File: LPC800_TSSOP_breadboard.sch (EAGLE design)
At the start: 16 parts, among them Q1 12MHz

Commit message: * small fixes on TODO list
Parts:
- added C6: (no value), SquantorRCL:C-EUC0603K
- C2, C3: device bart_rcl:C-EUC0603 -> SquantorRCL:C-EUC0603K
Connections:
- net VDD: now also C6.1
- net VSS: now also C6.2
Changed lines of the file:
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@@
 <grid distance="0.1" unitdist="inch" unit="inch" style="lines" multiple="1" display="no" altdistance="0.01" altunitdist="inch" altunit="inch"/>
 <layers>
-<layer number="1" name="Top" color="4" fill="1" visible="yes" active="no"/>
-<layer number="16" name="Bottom" color="1" fill="1" visible="yes" active="no"/>
-<layer number="17" name="Pads" color="2" fill="1" visible="yes" active="no"/>
-<layer number="18" name="Vias" color="2" fill="1" visible="yes" active="no"/>
-<layer number="19" name="Unrouted" color="6" fill="1" visible="yes" active="no"/>
-<layer number="20" name="Dimension" color="15" fill="1" visible="yes" active="no"/>
-<layer number="21" name="tPlace" color="7" fill="1" visible="yes" active="no"/>
-<layer number="22" name="bPlace" color="7" fill="1" visible="yes" active="no"/>
-<layer number="23" name="tOrigins" color="15" fill="1" visible="yes" active="no"/>
-<layer number="24" name="bOrigins" color="15" fill="1" visible="yes" active="no"/>
-<layer number="25" name="tNames" color="7" fill="1" visible="yes" active="no"/>
-<layer number="26" name="bNames" color="7" fill="1" visible="yes" active="no"/>
-<layer number="27" name="tValues" color="7" fill="1" visible="yes" active="no"/>
-<layer number="28" name="bValues" color="7" fill="1" visible="yes" active="no"/>
+<layer number="1" name="Top" color="4" fill="1" visible="no" active="no"/>
+<layer number="16" name="Bottom" color="1" fill="1" visible="no" active="no"/>
+<layer number="17" name="Pads" color="2" fill="1" visible="no" active="no"/>
+<layer number="18" name="Vias" color="2" fill="1" visible="no" active="no"/>
+<layer number="19" name="Unrouted" color="6" fill="1" visible="no" active="no"/>
+<layer number="20" name="Dimension" color="15" fill="1" visible="no" active="no"/>
+<layer number="21" name="tPlace" color="7" fill="1" visible="no" active="no"/>
+<layer number="22" name="bPlace" color="7" fill="1" visible="no" active="no"/>
+<layer number="23" name="tOrigins" color="15" fill="1" visible="no" active="no"/>
+<layer number="24" name="bOrigins" color="15" fill="1" visible="no" active="no"/>
+<layer number="25" name="tNames" color="7" fill="1" visible="no" active="no"/>
+<layer number="26" name="bNames" color="7" fill="1" visible="no" active="no"/>
+<layer number="27" name="tValues" color="7" fill="1" visible="no" active="no"/>
+<layer number="28" name="bValues" color="7" fill="1" visible="no" active="no"/>
 <layer number="29" name="tStop" color="7" fill="3" visible="no" active="no"/>
 <layer number="30" name="bStop" color="7" fill="6" visible="no" active="no"/>
@@
 <layer number="35" name="tGlue" color="7" fill="4" visible="no" active="no"/>
 <layer number="36" name="bGlue" color="7" fill="5" visible="no" active="no"/>
-<layer number="37" name="tTest" color="7" fill="1" visible="yes" active="no"/>
-<layer number="38" name="bTest" color="7" fill="1" visible="yes" active="no"/>
+<layer number="37" name="tTest" color="7" fill="1" visible="no" active="no"/>
+<layer number="38" name="bTest" color="7" fill="1" visible="no" active="no"/>
 <layer number="39" name="tKeepout" color="4" fill="11" visible="no" active="no"/>
 <layer number="40" name="bKeepout" color="1" fill="11" visible="no" active="no"/>
@@
 <layer number="44" name="Drills" color="7" fill="1" visible="no" active="no"/>
 <layer number="45" name="Holes" color="7" fill="1" visible="no" active="no"/>
-<layer number="46" name="Milling" color="3" fill="1" visible="yes" active="no"/>
-<layer number="47" name="Measures" color="7" fill="1" visible="yes" active="no"/>
-<layer number="48" name="Document" color="7" fill="1" visible="yes" active="no"/>
-<layer number="49" name="Reference" color="7" fill="1" visible="yes" active="no"/>
-<layer number="50" name="dxf" color="7" fill="1" visible="yes" active="no"/>
-<layer number="51" name="tDocu" color="7" fill="1" visible="yes" active="no"/>
-<layer number="52" name="bDocu" color="7" fill="1" visible="yes" active="no"/>
-<layer number="53" name="tGND_GNDA" color="7" fill="9" visible="yes" active="no"/>
-<layer number="54" name="bGND_GNDA" color="1" fill="9" visible="yes" active="no"/>
-<layer number="56" name="wert" color="7" fill="1" visible="yes" active="no"/>
+<layer number="46" name="Milling" color="3" fill="1" visible="no" active="no"/>
+<layer number="47" name="Measures" color="7" fill="1" visible="no" active="no"/>
+<layer number="48" name="Document" color="7" fill="1" visible="no" active="no"/>
+<layer number="49" name="Reference" color="7" fill="1" visible="no" active="no"/>
+<layer number="50" name="dxf" color="7" fill="1" visible="no" active="no"/>
+<layer number="51" name="tDocu" color="7" fill="1" visible="no" active="no"/>
+<layer number="52" name="bDocu" color="7" fill="1" visible="no" active="no"/>
+<layer number="53" name="tGND_GNDA" color="7" fill="9" visible="no" active="no"/>
+<layer number="54" name="bGND_GNDA" color="1" fill="9" visible="no" active="no"/>
+<layer number="56" name="wert" color="7" fill="1" visible="no" active="no"/>
 <layer number="91" name="Nets" color="2" fill="1" visible="yes" active="yes"/>
 <layer number="92" name="Busses" color="1" fill="1" visible="yes" active="yes"/>
@@
 <part name="C1" library="bart_rcl" deviceset="C-EU" device="C0402K" value="100n"/>
 <part name="Q1" library="bart_crystals" deviceset="CRYSTAL" device="SMD_5.0X3.2" value="12MHz"/>
-<part name="C2" library="bart_rcl" deviceset="C-EU" device="C0603" value="22p"/>
-<part name="C3" library="bart_rcl" deviceset="C-EU" device="C0603" value="22p"/>
+<part name="C2" library="SquantorRCL" deviceset="C-EU" device="C0603K" value="22p"/>
+<part name="C3" library="SquantorRCL" deviceset="C-EU" device="C0603K" value="22p"/>
 <part name="VSS1" library="supply1" deviceset="VSS" device=""/>
 <part name="VDD1" library="supply1" deviceset="VDD" device=""/>
@@
 <part name="U$3" library="bart_btn" deviceset="TACT_4PIN" device="KMR2" value="RESET"/>
 <part name="U$4" library="bart_btn" deviceset="TACT_4PIN" device="KMR2" value="ISP"/>
+<part name="C6" library="SquantorRCL" deviceset="C-EU" device="C0603K"/>
+<part name="VDD8" library="supply1" deviceset="VDD" device=""/>
+<part name="VSS11" library="supply1" deviceset="VSS" device=""/>
 </parts>
 <sheets>
@@
 <instance part="U$3" gate="G$1" x="172.72" y="66.04"/>
 <instance part="U$4" gate="G$1" x="172.72" y="45.72"/>
+<instance part="C6" gate="G$1" x="27.94" y="10.16"/>
+<instance part="VDD8" gate="G$1" x="27.94" y="17.78"/>
+<instance part="VSS11" gate="G$1" x="27.94" y="0"/>
 </instances>
 <busses>
@@
 <junction x="187.96" y="45.72"/>
 </segment>
+<segment>
+<pinref part="C6" gate="G$1" pin="2"/>
+<pinref part="VSS11" gate="G$1" pin="VSS"/>
+<wire x1="27.94" y1="5.08" x2="27.94" y2="2.54" width="0.1524" layer="91"/>
+</segment>
 </net>
 <net name="VDD" class="0">
@@
 <pinref part="VDD7" gate="G$1" pin="VDD"/>
 </segment>
+<segment>
+<pinref part="C6" gate="G$1" pin="1"/>
+<pinref part="VDD8" gate="G$1" pin="VDD"/>
+<wire x1="27.94" y1="12.7" x2="27.94" y2="15.24" width="0.1524" layer="91"/>
+</segment>
 </net>

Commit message: * updated board and schem with todo's
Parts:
- removed JP1, JP2: (no value), bart_connectors:PINHD-1X11TH_SMALL
- added JP4, JP5: (no value), SquantorConnectors:PINHD-1X12SMALL
- C4, C5: device bart_rcl:C-EUC0805 -> bart_rcl:C-EUC0805K
- renumbered LOGO1 to LOGO2
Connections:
- net PIO0_0: now also JP4.9; no longer JP1.9
- net PIO0_1: now also JP4.2; no longer JP1.2
- net PIO0_10: now also JP5.11; no longer JP2.10
- net PIO0_11: now also JP5.10; no longer JP2.9
- net PIO0_12: now also JP5.5; no longer JP2.4
- net PIO0_13: now also JP5.4; no longer JP2.3
- net PIO0_14: now also JP4.10; no longer JP1.10
- net PIO0_15: now also JP4.1; no longer JP1.1
- net PIO0_16: now also JP5.12; no longer JP2.11
- net PIO0_17: now also JP5.3; no longer JP2.2
- net PIO0_2: now also JP5.9; no longer JP2.8
- net PIO0_3: now also JP5.8; no longer JP2.7
- net PIO0_4: now also JP5.7; no longer JP2.6
- net PIO0_5: now also JP5.6; no longer JP2.5
- net PIO0_6: now also JP4.8; no longer JP1.8
- net PIO0_7: now also JP4.7; no longer JP1.7
- net PIO0_8: now also JP4.4; no longer JP1.4
- net PIO0_9: now also JP4.3; no longer JP1.3
- net VCCIO: now also JP4.12; no longer JP2.1
- net VDD: now also JP4.5, JP5.1; no longer JP1.5
- net VSS: now also JP4.11, JP4.6, JP5.2; no longer JP1.11, JP1.6

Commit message: * minor updates with silk, pinout documentation, hole expansion
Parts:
- removed C1: 100n, bart_rcl:C-EUC0402K
- JP4, JP5: device SquantorConnectors:PINHD-1X12SMALL -> SquantorConnectors:PINHD-1X12NORM_OCT
- renumbered U$1 to LPC812
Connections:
- net VDD: no longer C1.1
- net VSS: no longer C1.2

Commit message: * small modifications * improved regulator decoupling capacitor position to leave more space for the pinheaders * improved crystal positioning to leave more space for the pinheaders
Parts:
- U$3, U$4: device bart_btn:TACT_4PINKMR2 -> SquantorButtons:TACT_4PINKMR2
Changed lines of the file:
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@@
 <part name="VDD6" library="supply1" deviceset="VDD" device=""/>
 <part name="VDD7" library="supply1" deviceset="VDD" device=""/>
-<part name="U$3" library="bart_btn" deviceset="TACT_4PIN" device="KMR2" value="RESET"/>
-<part name="U$4" library="bart_btn" deviceset="TACT_4PIN" device="KMR2" value="ISP"/>
+<part name="U$3" library="SquantorButtons" deviceset="TACT_4PIN" device="KMR2" value="RESET"/>
+<part name="U$4" library="SquantorButtons" deviceset="TACT_4PIN" device="KMR2" value="ISP"/>
 <part name="C6" library="SquantorRCL" deviceset="C-EU" device="C0603K"/>
 <part name="VDD8" library="supply1" deviceset="VDD" device=""/>

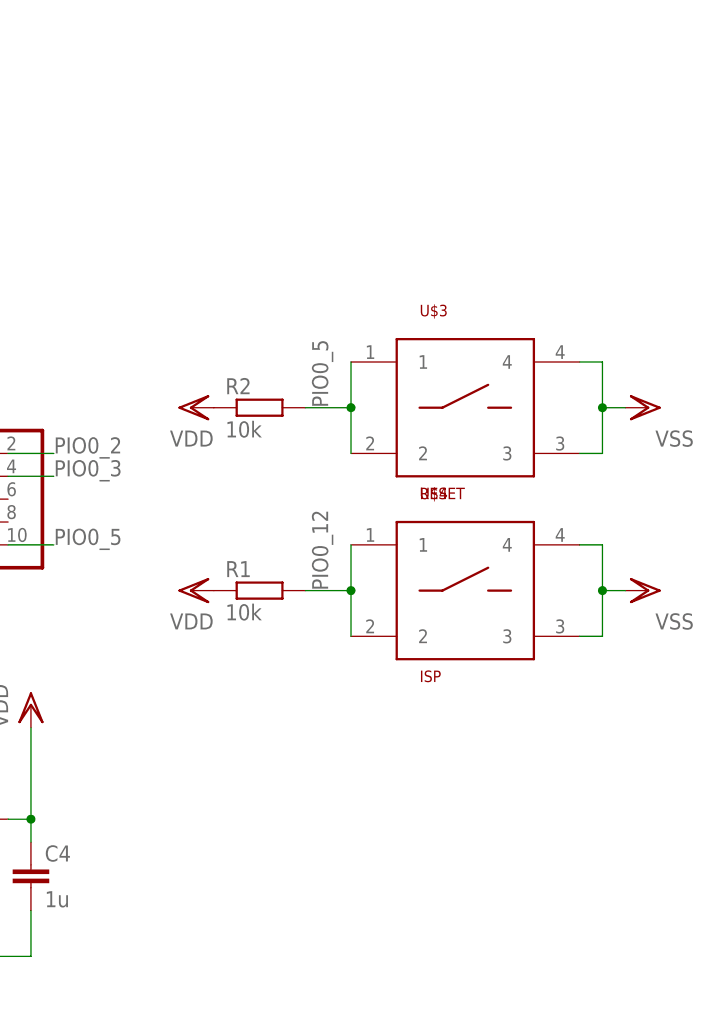
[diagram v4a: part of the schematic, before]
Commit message: * updated boards with cheaper buttons, better layout and indexed JTAG header
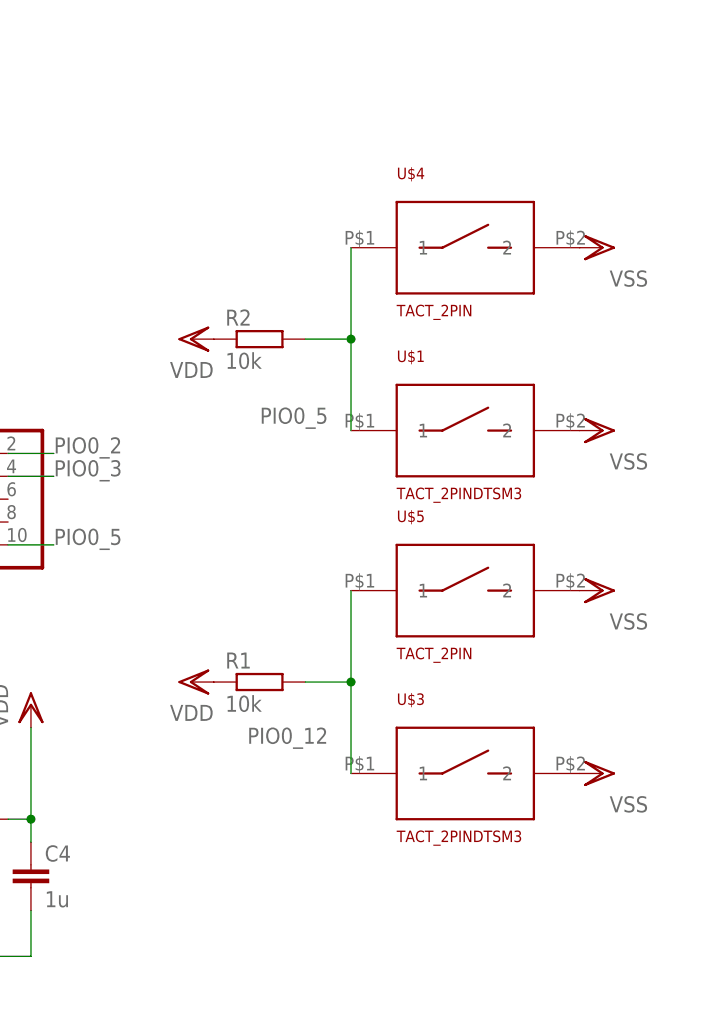
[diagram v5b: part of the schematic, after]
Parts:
- added U$1: TACT_2PINDTSM3, SquantorButtons:TACT_2PINDTSM3
- added U$5: TACT_2PIN, SquantorButtons:TACT_2PIN
- JP3: device bart_connectors:PINHD-2X5SMD_1.27_SMD -> SquantorConnectors:PINHD-2X5SMD_1.27_SMD
- U$3: value RESET -> TACT_2PINDTSM3; device SquantorButtons:TACT_4PINKMR2 -> SquantorButtons:TACT_2PINDTSM3
- U$4: value ISP -> TACT_2PIN; device SquantorButtons:TACT_4PINKMR2 -> SquantorButtons:TACT_2PIN
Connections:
- net PIO0_12: now also U$3.1, U$5.1; no longer U$4.1, U$4.2
- net PIO0_5: now also U$1.1, U$4.1; no longer U$3.1, U$3.2
- net VSS: now also U$1.2, U$3.2, U$4.2, U$5.2; no longer U$3.3, U$3.4, U$4.3, U$4.4
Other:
- moved on the sheet: R1, R2
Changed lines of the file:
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@@
 <part name="VSS5" library="supply1" deviceset="VSS" device=""/>
 <part name="VDD3" library="supply1" deviceset="VDD" device=""/>
-<part name="JP3" library="bart_connectors" deviceset="PINHD-2X5" device="SMD_1.27_SMD" value="JTAG"/>
+<part name="JP3" library="SquantorConnectors" deviceset="PINHD-2X5" device="SMD_1.27_SMD" value="JTAG"/>
 <part name="VDD4" library="supply1" deviceset="VDD" device=""/>
 <part name="VSS6" library="supply1" deviceset="VSS" device=""/>
@@
 <part name="VSS8" library="supply1" deviceset="VSS" device=""/>
 <part name="VDD2" library="supply1" deviceset="VDD" device=""/>
-<part name="VSS9" library="supply1" deviceset="VSS" device=""/>
 <part name="VSS10" library="supply1" deviceset="VSS" device=""/>
 <part name="R1" library="bart_rcl" deviceset="R-EU_" device="R0603" value="10k"/>
@@
 <part name="VDD6" library="supply1" deviceset="VDD" device=""/>
 <part name="VDD7" library="supply1" deviceset="VDD" device=""/>
-<part name="U$3" library="SquantorButtons" deviceset="TACT_4PIN" device="KMR2" value="RESET"/>
-<part name="U$4" library="SquantorButtons" deviceset="TACT_4PIN" device="KMR2" value="ISP"/>
 <part name="C6" library="SquantorRCL" deviceset="C-EU" device="C0603K"/>
 <part name="VDD8" library="supply1" deviceset="VDD" device=""/>
@@
 <part name="VDD9" library="supply1" deviceset="VDD" device=""/>
 <part name="VSS12" library="supply1" deviceset="VSS" device=""/>
+<part name="U$1" library="SquantorButtons" deviceset="TACT_2PIN" device="DTSM3"/>
+<part name="U$3" library="SquantorButtons" deviceset="TACT_2PIN" device="DTSM3"/>
+<part name="U$4" library="SquantorButtons" deviceset="TACT_2PIN" device=""/>
+<part name="U$5" library="SquantorButtons" deviceset="TACT_2PIN" device=""/>
+<part name="VSS1" library="supply1" deviceset="VSS" device=""/>
+<part name="VSS9" library="supply1" deviceset="VSS" device=""/>
+<part name="VSS13" library="supply1" deviceset="VSS" device=""/>
 </parts>
 <sheets>
@@
 <instance part="VSS8" gate="G$1" x="55.88" y="71.12" rot="R270"/>
 <instance part="VDD2" gate="G$1" x="63.5" y="55.88" rot="R90"/>
-<instance part="VSS9" gate="G$1" x="193.04" y="66.04" rot="R90"/>
-<instance part="VSS10" gate="G$1" x="193.04" y="45.72" rot="R90"/>
-<instance part="R1" gate="G$1" x="149.86" y="45.72"/>
-<instance part="R2" gate="G$1" x="149.86" y="66.04"/>
-<instance part="VDD6" gate="G$1" x="142.24" y="45.72" rot="R90"/>
-<instance part="VDD7" gate="G$1" x="142.24" y="66.04" rot="R90"/>
-<instance part="U$3" gate="G$1" x="172.72" y="66.04"/>
-<instance part="U$4" gate="G$1" x="172.72" y="45.72"/>
+<instance part="VSS10" gate="G$1" x="187.96" y="45.72" rot="R90"/>
+<instance part="R1" gate="G$1" x="149.86" y="35.56"/>
+<instance part="R2" gate="G$1" x="149.86" y="73.66"/>
+<instance part="VDD6" gate="G$1" x="142.24" y="35.56" rot="R90"/>
+<instance part="VDD7" gate="G$1" x="142.24" y="73.66" rot="R90"/>
 <instance part="C6" gate="G$1" x="27.94" y="10.16"/>
 <instance part="VDD8" gate="G$1" x="27.94" y="17.78"/>
@@
 <instance part="VDD9" gate="G$1" x="35.56" y="73.66" rot="R270"/>
 <instance part="VSS12" gate="G$1" x="35.56" y="71.12" rot="R90"/>
+<instance part="U$1" gate="G$1" x="172.72" y="63.5"/>
+<instance part="U$3" gate="G$1" x="172.72" y="25.4"/>
+<instance part="U$4" gate="G$1" x="172.72" y="83.82"/>
+<instance part="U$5" gate="G$1" x="172.72" y="45.72"/>
+<instance part="VSS1" gate="G$1" x="187.96" y="63.5" rot="R90"/>
+<instance part="VSS9" gate="G$1" x="187.96" y="83.82" rot="R90"/>
+<instance part="VSS13" gate="G$1" x="187.96" y="25.4" rot="R90"/>
 </instances>
 <busses>
@@
 </segment>
 <segment>
-<pinref part="U$3" gate="G$1" pin="4"/>
-<wire x1="185.42" y1="71.12" x2="187.96" y2="71.12" width="0.1524" layer="91"/>
-<wire x1="187.96" y1="71.12" x2="187.96" y2="66.04" width="0.1524" layer="91"/>
-<pinref part="VSS9" gate="G$1" pin="VSS"/>
-<wire x1="187.96" y1="66.04" x2="190.5" y2="66.04" width="0.1524" layer="91"/>
-<pinref part="U$3" gate="G$1" pin="3"/>
-<wire x1="185.42" y1="60.96" x2="187.96" y2="60.96" width="0.1524" layer="91"/>
-<wire x1="187.96" y1="60.96" x2="187.96" y2="66.04" width="0.1524" layer="91"/>
-<junction x="187.96" y="66.04"/>
-</segment>
-<segment>
-<pinref part="U$4" gate="G$1" pin="4"/>
-<wire x1="185.42" y1="50.8" x2="187.96" y2="50.8" width="0.1524" layer="91"/>
-<wire x1="187.96" y1="50.8" x2="187.96" y2="45.72" width="0.1524" layer="91"/>
-<pinref part="VSS10" gate="G$1" pin="VSS"/>
-<wire x1="187.96" y1="45.72" x2="190.5" y2="45.72" width="0.1524" layer="91"/>
-<pinref part="U$4" gate="G$1" pin="3"/>
-<wire x1="185.42" y1="40.64" x2="187.96" y2="40.64" width="0.1524" layer="91"/>
-<wire x1="187.96" y1="40.64" x2="187.96" y2="45.72" width="0.1524" layer="91"/>
-<junction x="187.96" y="45.72"/>
-</segment>
-<segment>
 <pinref part="C6" gate="G$1" pin="2"/>
 <pinref part="VSS11" gate="G$1" pin="VSS"/>
@@
 <pinref part="JP4" gate="G$1" pin="11"/>
 <wire x1="58.42" y1="71.12" x2="66.04" y2="71.12" width="0.1524" layer="91"/>
+</segment>
+<segment>
+<pinref part="U$1" gate="G$1" pin="2"/>
+<pinref part="VSS1" gate="G$1" pin="VSS"/>
+</segment>
+<segment>
+<pinref part="U$4" gate="G$1" pin="2"/>
+<pinref part="VSS9" gate="G$1" pin="VSS"/>
+</segment>
+<segment>
+<pinref part="U$3" gate="G$1" pin="2"/>
+<pinref part="VSS13" gate="G$1" pin="VSS"/>
+</segment>
+<segment>
+<pinref part="U$5" gate="G$1" pin="2"/>
+<pinref part="VSS10" gate="G$1" pin="VSS"/>
 </segment>
 </net>
@@
 <segment>
 <pinref part="R2" gate="G$1" pin="2"/>
-<wire x1="154.94" y1="66.04" x2="160.02" y2="66.04" width="0.1524" layer="91"/>
-<label x="157.48" y="66.04" size="1.778" layer="95" rot="R90"/>
-<pinref part="U$3" gate="G$1" pin="2"/>
-<wire x1="160.02" y1="66.04" x2="160.02" y2="60.96" width="0.1524" layer="91"/>
-<pinref part="U$3" gate="G$1" pin="1"/>
-<wire x1="160.02" y1="71.12" x2="160.02" y2="66.04" width="0.1524" layer="91"/>
-<junction x="160.02" y="66.04"/>
+<wire x1="154.94" y1="73.66" x2="160.02" y2="73.66" width="0.1524" layer="91"/>
+<label x="157.48" y="66.04" size="1.778" layer="95" rot="R180"/>
+<wire x1="160.02" y1="73.66" x2="160.02" y2="63.5" width="0.1524" layer="91"/>
+<wire x1="160.02" y1="83.82" x2="160.02" y2="73.66" width="0.1524" layer="91"/>
+<junction x="160.02" y="73.66"/>
+<pinref part="U$1" gate="G$1" pin="1"/>
+<pinref part="U$4" gate="G$1" pin="1"/>
 </segment>
 </net>
@@
 <segment>
 <pinref part="R1" gate="G$1" pin="2"/>
-<wire x1="154.94" y1="45.72" x2="160.02" y2="45.72" width="0.1524" layer="91"/>
-<label x="157.48" y="45.72" size="1.778" layer="95" rot="R90"/>
-<pinref part="U$4" gate="G$1" pin="1"/>
-<wire x1="160.02" y1="45.72" x2="160.02" y2="50.8" width="0.1524" layer="91"/>
-<pinref part="U$4" gate="G$1" pin="2"/>
-<wire x1="160.02" y1="40.64" x2="160.02" y2="45.72" width="0.1524" layer="91"/>
-<junction x="160.02" y="45.72"/>
-</segment>
-</net>
+<label x="157.48" y="30.48" size="1.778" layer="95" rot="R180"/>
+<wire x1="160.02" y1="25.4" x2="160.02" y2="35.56" width="0.1524" layer="91"/>
+<pinref part="U$3" gate="G$1" pin="1"/>
+<pinref part="U$5" gate="G$1" pin="1"/>
+<wire x1="160.02" y1="35.56" x2="160.02" y2="45.72" width="0.1524" layer="91"/>
+<wire x1="154.94" y1="35.56" x2="160.02" y2="35.56" width="0.1524" layer="91"/>
+<junction x="160.02" y="35.56"/>
+</segment>
+</net>

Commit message: * small changes preparing for commit to OSH park
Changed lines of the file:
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@@
 <?xml version="1.0" encoding="utf-8"?>
 <!DOCTYPE eagle SYSTEM "eagle.dtd">
-<eagle version="6.5.0">
+<eagle version="7.1.0">
 <drawing>
 <settings>
@@
 <segment>
 <pinref part="JP3" gate="A" pin="2"/>
-<wire x1="121.92" y1="60.96" x2="127" y2="60.96" width="0.1524" layer="91"/>
-<label x="127" y="60.96" size="1.778" layer="95"/>
+<wire x1="121.92" y1="60.96" x2="137.16" y2="60.96" width="0.1524" layer="91"/>
+<label x="137.16" y="60.96" size="1.778" layer="95"/>
 </segment>
 </net>
@@
 <segment>
 <pinref part="JP3" gate="A" pin="4"/>
-<wire x1="121.92" y1="58.42" x2="127" y2="58.42" width="0.1524" layer="91"/>
-<label x="127" y="58.42" size="1.778" layer="95"/>
+<wire x1="121.92" y1="58.42" x2="137.16" y2="58.42" width="0.1524" layer="91"/>
+<label x="137.16" y="58.42" size="1.778" layer="95"/>
 </segment>
 </net>
@@
 <pinref part="JP3" gate="A" pin="10"/>
 <wire x1="121.92" y1="50.8" x2="127" y2="50.8" width="0.1524" layer="91"/>
-<label x="127" y="50.8" size="1.778" layer="95"/>
-</segment>
-<segment>
+<wire x1="127" y1="50.8" x2="127" y2="43.18" width="0.1524" layer="91"/>
+<label x="127" y="43.18" size="1.778" layer="95" rot="R270"/>
+</segment>
+<segment>
